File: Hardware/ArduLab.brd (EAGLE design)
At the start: 80 x 100 mm, 94 parts, among them CN1 USB-B, CN2 JST-PH, T1 MMUN2133LT1G, U1 ATMEGA32U4-AU, U2 MIC5205, U3 TPS61030PWP, U4 MCP73831, U5 L293DD, X1 16MHz

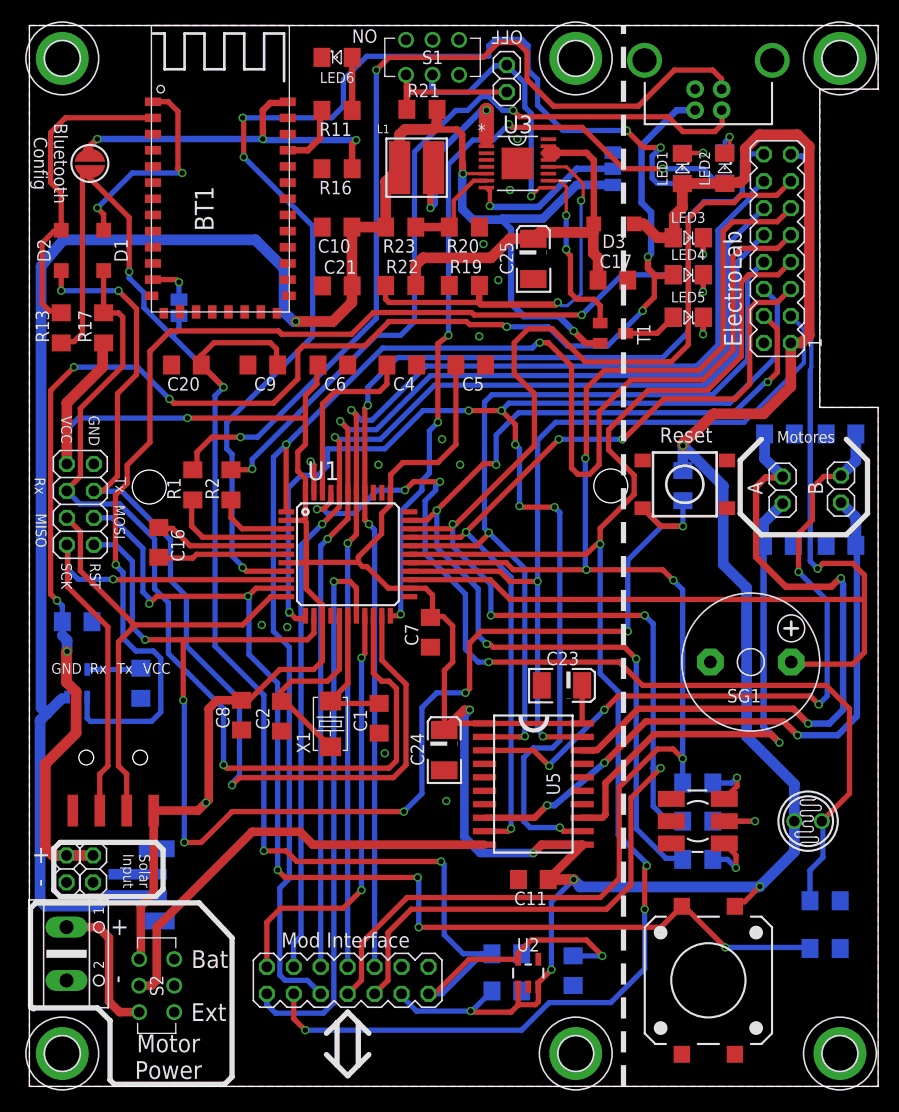
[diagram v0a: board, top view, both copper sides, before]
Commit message: Fixed bug: Battery connector polarity
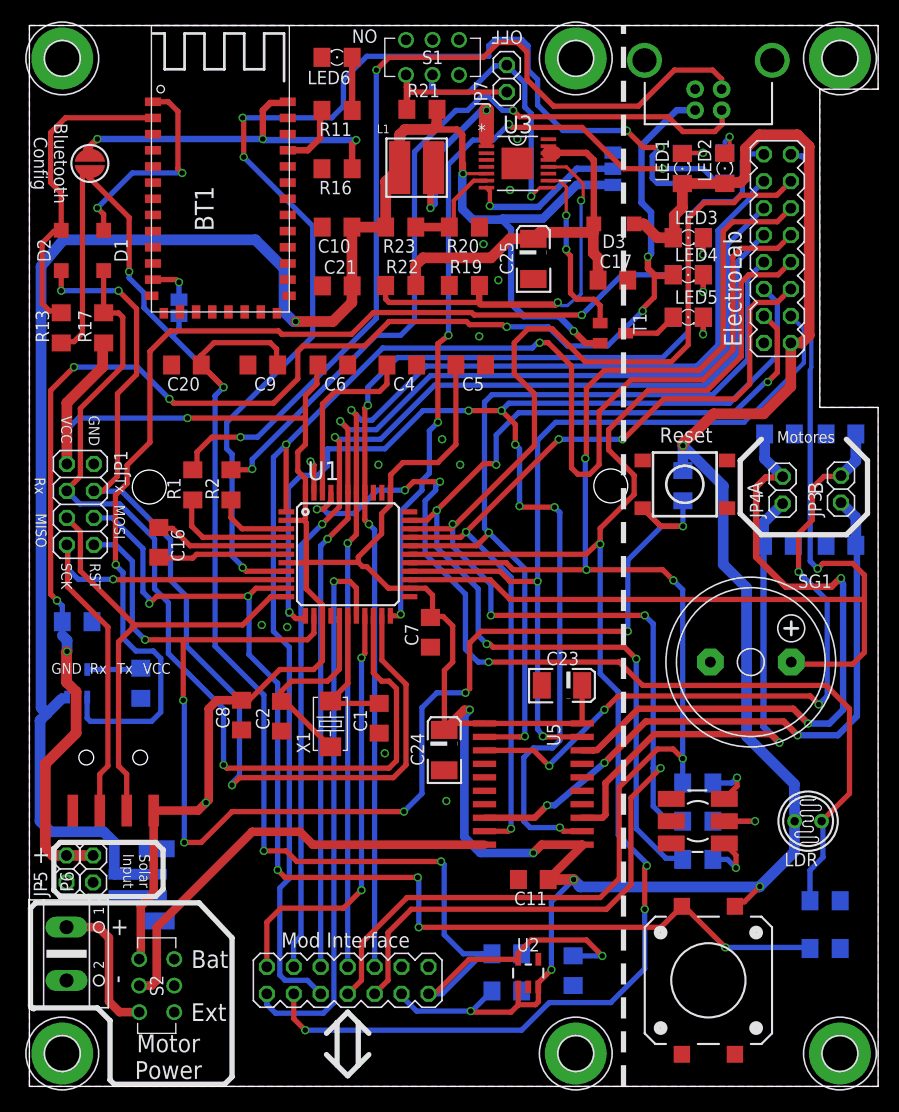
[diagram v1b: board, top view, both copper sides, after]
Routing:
- net VBAT: track 179.8 -> 178.2 mm

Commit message: Modified: Center pad of U3 (TPS61030) wired to ground
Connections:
- net GND: now also U3.17
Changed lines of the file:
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@@
 <layer number="25" name="tNames" color="7" fill="1" visible="yes" active="yes"/>
 <layer number="26" name="bNames" color="7" fill="1" visible="yes" active="yes"/>
-<layer number="27" name="tValues" color="7" fill="1" visible="yes" active="yes"/>
+<layer number="27" name="tValues" color="7" fill="1" visible="no" active="yes"/>
 <layer number="28" name="bValues" color="7" fill="1" visible="yes" active="yes"/>
 <layer number="29" name="tStop" color="7" fill="3" visible="yes" active="yes"/>
@@
 <contactref element="C21" pad="1"/>
 <contactref element="CN2" pad="1"/>
+<contactref element="U3" pad="17"/>
 </signal>
 <signal name="AREF">

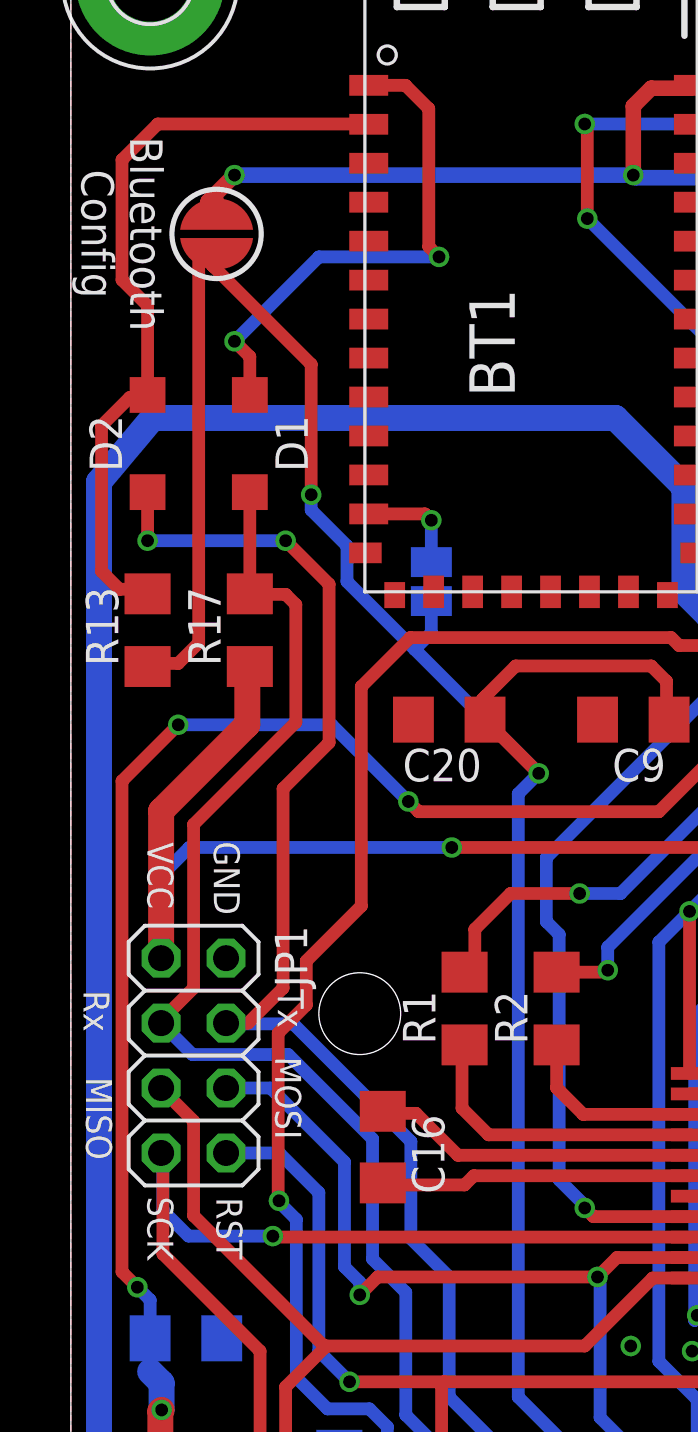
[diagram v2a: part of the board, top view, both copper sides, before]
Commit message: Bluetooth-microcontroller communication improved with shift level conversor.
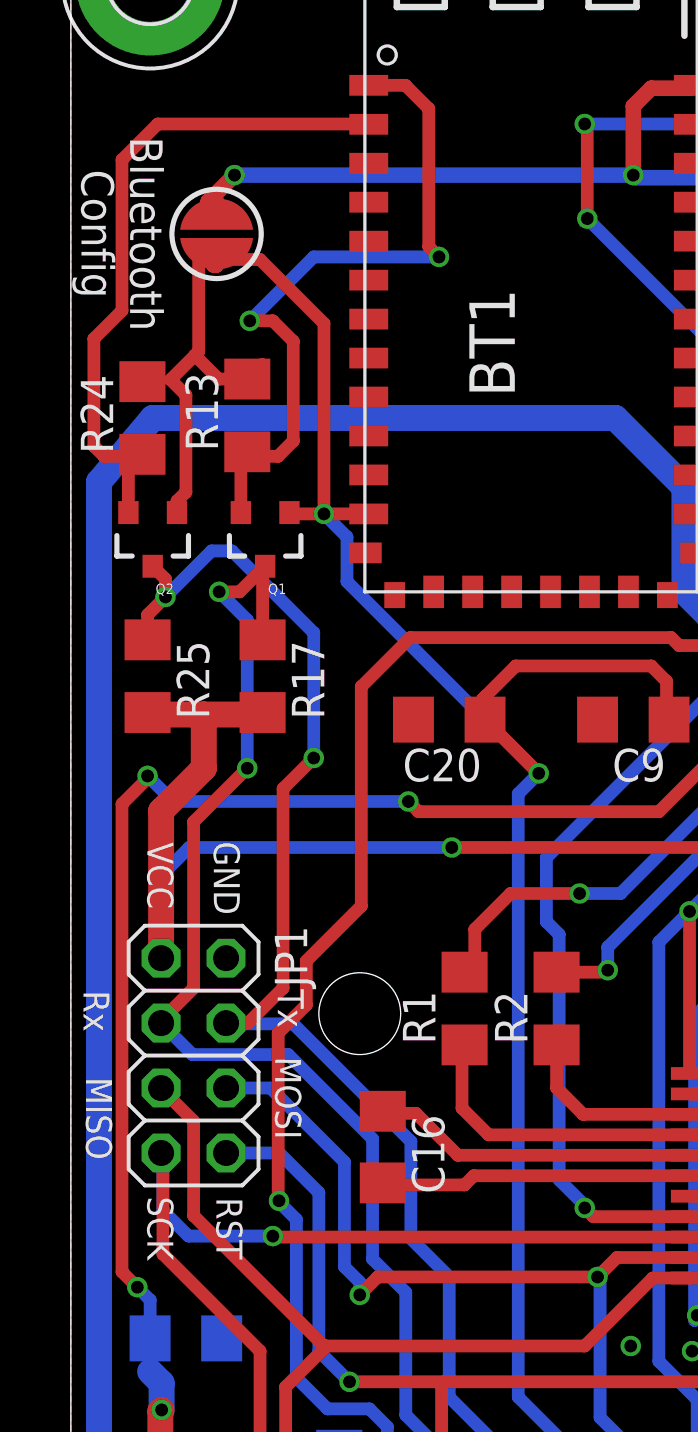
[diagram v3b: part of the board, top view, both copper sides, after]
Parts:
- removed D1, D2: 5819, diode:SOD123
- removed SJ3: (no value), jumper:SJ
- added Q1, Q2: BSS138, SparkFun:SOT23-3
- added R24, R25: 10K, resistor:R1206
- R13: value 4.7k -> 10K
- R17: value 10k -> 10K
- moved R13 9.26 mm to (6.90, 79.9)
- moved R17 1.87 mm to (7.50, 69.7), turned to 270 degrees
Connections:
- removed net N$20: BT1.1, D1.C
- removed net N$21: BT1.2, D2.A, R13.2
- removed net N$7: BT1.12, SJ3.2
- new net BRX: BT1.2, Q2.2, R24.1
- new net BTX: BT1.1, Q1.2, R13.1
- net 3.3V: now also BT1.12, Q1.1, Q2.1, R13.2, R24.2; no longer R13.1, SJ3.1
- net D0: now also Q1.3, R17.1; no longer D1.A, R17.2
- net D1: now also Q2.3, R25.1; no longer D2.C
- net GND: now also BT1.14, BT1.21
- net VCC: now also R17.2, R25.2; no longer R17.1
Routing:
- net N$21: track 30.0 -> 0.00 mm
- net BTX: track 0.00 -> 27.7 mm, vias 0 -> 2
- net BRX: track 0.00 -> 26.5 mm
- net N$20: track 20.4 -> 0.00 mm, vias 2 -> 0
- net N$7: track 4.19 -> 0.00 mm, vias 1 -> 0
- net VBUS: track 143.7 -> 141.6 mm
- net VCC: track 396.1 -> 398.1 mm
- net 3.3V: track 168.2 -> 167.1 mm
- net D0: track 90.3 -> 89.7 mm, vias 1 -> 3
- net D1: track 96.5 -> 95.9 mm
